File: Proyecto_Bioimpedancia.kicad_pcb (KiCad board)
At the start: 2 copper layers, 100 x 100 mm, 76 parts, among them J1 Jumper, J2 Jumper, J3 Jumper_Calibration, J4 Jumper, J5 Jumper, J6 Jumper, P1 SD_LAPIZ, P10 UNIVERSAL_PINS, P11 SOURCE_2, P12 RESET, P13 POWER, P14 BIO_OUT1, P15 GND_REGULATOR, P16 BIO_OUT2, P17 TOR_1, P18 TOR_2, P19 TOR_3, P2 GPIO, P20 TOR_4, P3 SOURCE_3, P4 SERIAL_VIRTUAL, P5 ENCODER, P6 I2C, P7 CONN_01X04, P8 SOURCE_1, P9 SPI, SW1 SW_PUSH, U1 AD8606, U2 ADG819, U3 Atmega328PA, U4 LD1117S50TR, Y1 XRCHA_16M

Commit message: Logos y Nombre de la Placa
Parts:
- added G***: LOGO, Logos_Fuentes:UIS, F.Cu at (92.7, 121.3)
- added G***: LOGO, Logos_Fuentes:CMOS, F.Cu at (92.9, 111.8)
- added G***: LOGO, Logos_Fuentes:Colombia, F.Cu at (93.0, 131.1)
- added G***: LOGO, Logos_Fuentes:SBS, F.Cu at (152.6, 108.0)
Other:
- board text added: "1 BIOIMPEDANCEMETER"

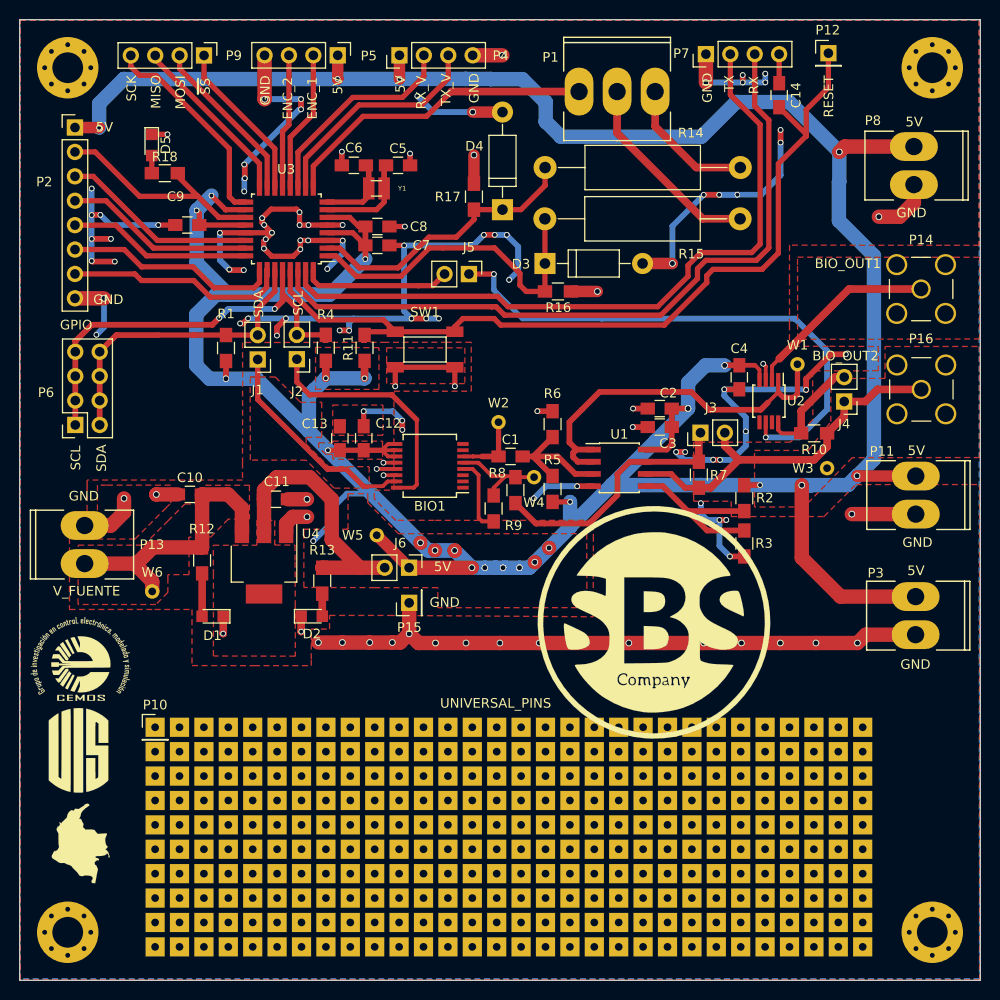
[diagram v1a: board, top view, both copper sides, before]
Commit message: Vias de PCB
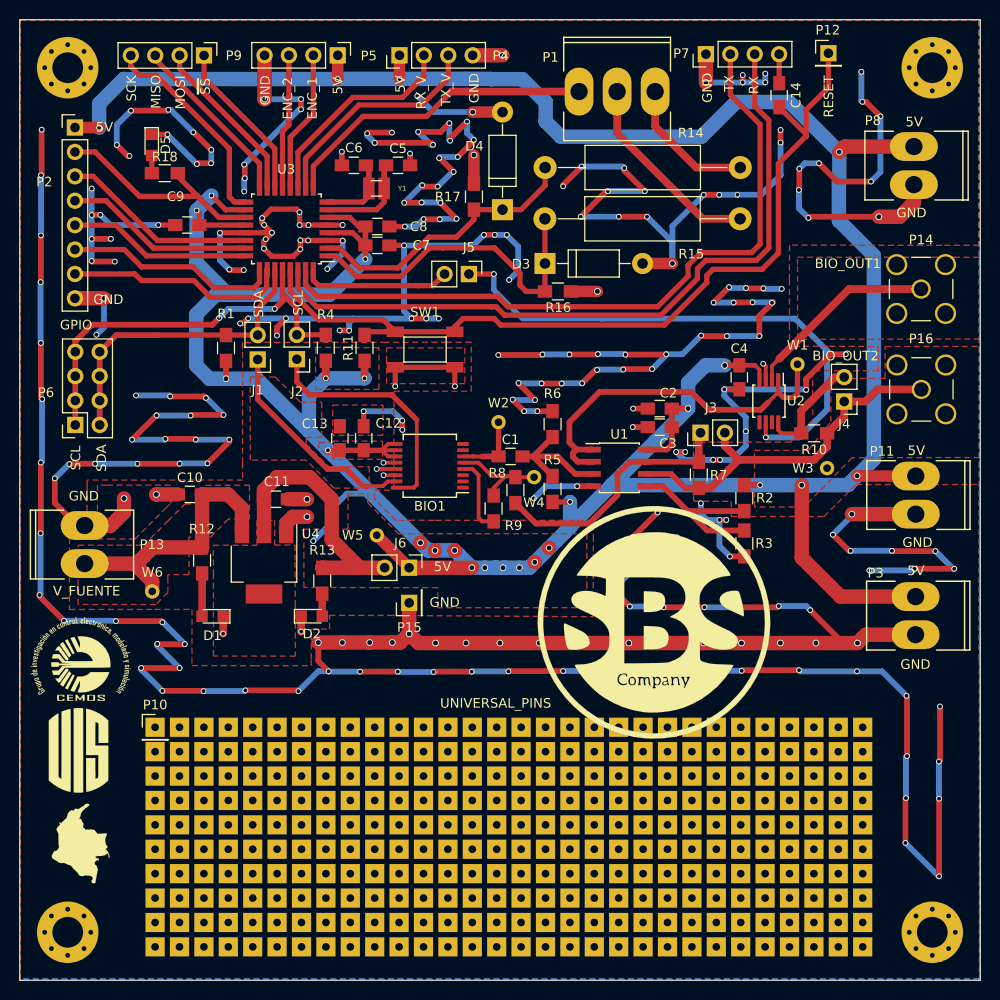
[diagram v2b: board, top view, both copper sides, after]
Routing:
- net /AGND: track 374.4 -> 917.6 mm, vias 118 -> 265
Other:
- board text added: "001 BIOIMPEDANCEMETER"
- board text removed: "1 BIOIMPEDANCEMETER"

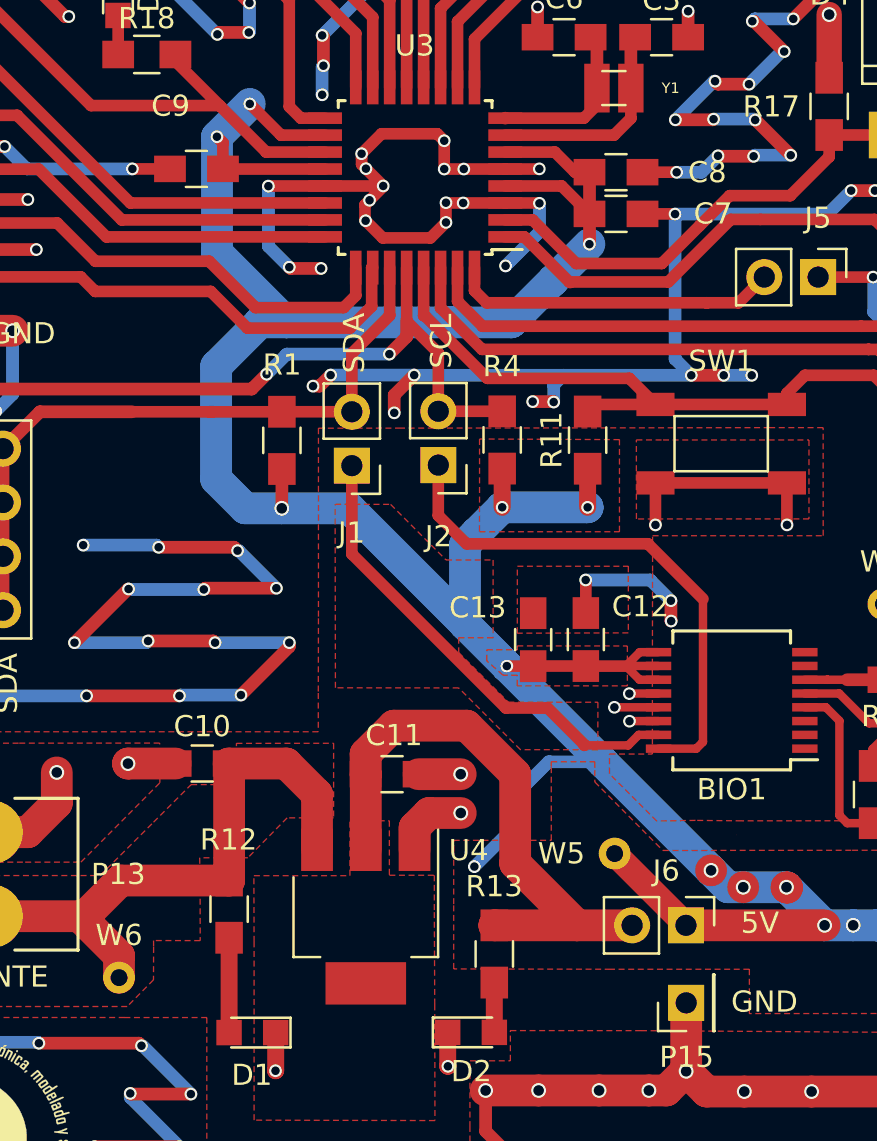
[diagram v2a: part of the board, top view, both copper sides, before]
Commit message: Planos de placa mejorados
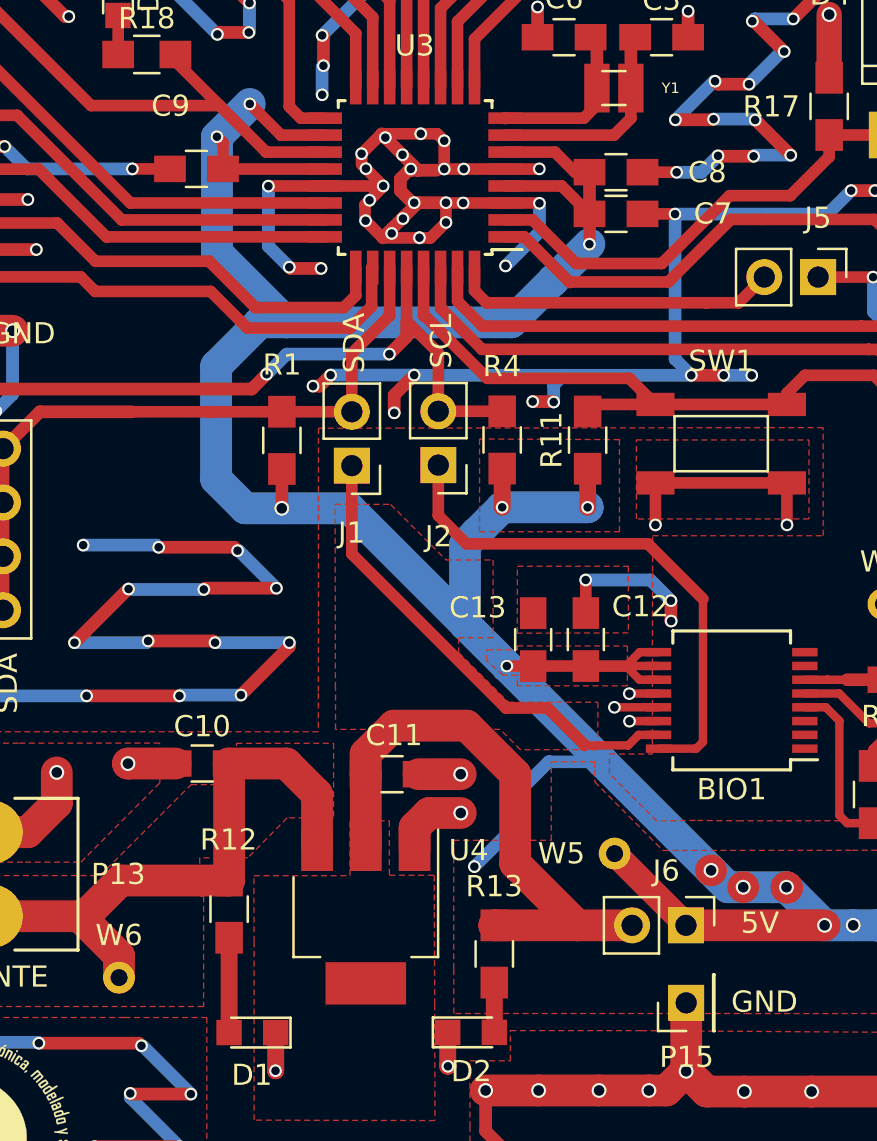
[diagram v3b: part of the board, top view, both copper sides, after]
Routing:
- net /AGND: track 917.6 -> 928.1 mm, vias 265 -> 273
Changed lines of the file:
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@@
     (thickness 1.6)
     (drawings 43)
-    (tracks 1368)
+    (tracks 1406)
     (zones 0)
     (modules 80)
@@
   (segment (start 132.70552 90.67836) (end 133.76438 90.67836) (width 0.4) (layer F.Cu) (net 3))
   (segment (start 133.76438 90.67836) (end 133.7691 90.68308) (width 0.4) (layer F.Cu) (net 3))
+  (via (at 114.53 69.83) (size 0.6) (drill 0.4) (layers F.Cu B.Cu) (net 5))
+  (segment (start 114.53 69.83) (end 114.53 69.85) (width 0.6) (layer B.Cu) (net 5))
+  (segment (start 114.53 69.83) (end 114.53 69.84) (width 0.6) (layer F.Cu) (net 5))
+  (segment (start 114.53 69.83) (end 114.53 69.84) (width 0.6) (layer F.Cu) (net 5))
+  (via (at 114.59 64.93) (size 0.6) (drill 0.4) (layers F.Cu B.Cu) (net 5))
+  (segment (start 114.59 64.93) (end 114.59 64.92) (width 0.6) (layer B.Cu) (net 5))
+  (segment (start 113.22 69.62) (end 113.22 69.63) (width 0.6) (layer B.Cu) (net 5))
+  (via (at 113.22 69.63) (size 0.6) (drill 0.4) (layers F.Cu B.Cu) (net 5))
+  (segment (start 113.22 69.63) (end 113.115 69.525) (width 0.6) (layer F.Cu) (net 5))
+  (segment (start 113.115 69.525) (end 113.22 69.63) (width 0.6) (layer F.Cu) (net 5))
+  (segment (start 113.22 69.63) (end 113.22 69.42) (width 0.6) (layer F.Cu) (net 5))
+  (via (at 112.92 65.11) (size 0.6) (drill 0.4) (layers F.Cu B.Cu) (net 5))
+  (via (at 113.75 68.93) (size 0.6) (drill 0.4) (layers F.Cu B.Cu) (net 5))
+  (segment (start 113.75 68.89) (end 113.75 68.93) (width 0.6) (layer F.Cu) (net 5))
+  (segment (start 113.73 68.91) (end 113.75 68.93) (width 0.6) (layer F.Cu) (net 5))
+  (segment (start 113.75 68.93) (end 113.73 68.91) (width 0.6) (layer F.Cu) (net 5))
+  (via (at 113.73 65.92) (size 0.6) (drill 0.4) (layers F.Cu B.Cu) (net 5))
+  (via (at 114.12 66.59) (size 0.6) (drill 0.4) (layers F.Cu B.Cu) (net 5))
+  (segment (start 114.03 66.65) (end 114.12 66.65) (width 0.6) (layer F.Cu) (net 5))
+  (segment (start 114.12 66.65) (end 114.12 66.59) (width 0.6) (layer F.Cu) (net 5))
+  (via (at 114.28 68.18) (size 0.6) (drill 0.4) (layers F.Cu B.Cu) (net 5))
+  (segment (start 114.28 68.18) (end 114.28 68.17) (width 0.6) (layer B.Cu) (net 5))
+  (segment (start 114.46 68.18) (end 114.28 68.18) (width 0.6) (layer F.Cu) (net 5))
+  (segment (start 114.28 68.18) (end 114.19 68.18) (width 0.6) (layer F.Cu) (net 5))
+  (segment (start 114.03 66.65) (end 114.46 66.65) (width 0.6) (layer F.Cu) (net 5))
+  (segment (start 113.63 67.05) (end 114.03 66.65) (width 0.6) (layer F.Cu) (net 5))
+  (segment (start 113.63 67.62) (end 113.63 67.05) (width 0.6) (layer F.Cu) (net 5))
+  (segment (start 114.19 68.18) (end 113.63 67.62) (width 0.6) (layer F.Cu) (net 5))
+  (segment (start 115.78 68.18) (end 114.46 68.18) (width 0.6) (layer F.Cu) (net 5))
+  (segment (start 114.46 68.18) (end 113.75 68.89) (width 0.6) (layer F.Cu) (net 5))
+  (segment (start 113.75 68.89) (end 113.22 69.42) (width 0.6) (layer F.Cu) (net 5))
+  (segment (start 113.22 69.42) (end 112.8 69.84) (width 0.6) (layer F.Cu) (net 5))
+  (segment (start 115.34 66.65) (end 114.46 66.65) (width 0.6) (layer F.Cu) (net 5))
+  (segment (start 114.46 66.65) (end 113.73 65.92) (width 0.6) (layer F.Cu) (net 5))
+  (segment (start 113.73 65.92) (end 112.92 65.11) (width 0.6) (layer F.Cu) (net 5))
+  (segment (start 112.92 65.11) (end 112.74 64.93) (width 0.6) (layer F.Cu) (net 5))
   (segment (start 173.18736 96.68256) (end 173.18736 96.85264) (width 0.6) (layer B.Cu) (net 5))
   (via (at 173.18736 96.68256) (size 0.7) (drill 0.5) (layers F.Cu B.Cu) (net 5))
@@
   (via (at 139.08 85.97) (size 0.6) (drill 0.4) (layers F.Cu B.Cu) (net 5))
   (segment (start 139.08624 85.96376) (end 139.08 85.97) (width 0.6) (layer B.Cu) (net 5))
-  (segment (start 93.325 97.8688) (end 92.5688 97.8688) (width 0.6) (layer F.Cu) (net 5) (status C00000))
-  (segment (start 92.5688 97.8688) (end 90.22 95.52) (width 0.6) (layer F.Cu) (net 5) (status 400000))
+  (segment (start 93.325 97.8688) (end 92.5688 97.8688) (width 0.6) (layer F.Cu) (net 5))
+  (segment (start 92.5688 97.8688) (end 90.22 95.52) (width 0.6) (layer F.Cu) (net 5))
   (via (at 98.67 84.33) (size 0.6) (drill 0.4) (layers F.Cu B.Cu) (net 5))
   (segment (start 102.13 84.33) (end 98.67 84.33) (width 0.6) (layer B.Cu) (net 5))
@@
   (via (at 111.8 65.87) (size 0.6) (drill 0.4) (layers F.Cu B.Cu) (net 5))
   (via (at 111.99 69.03) (size 0.6) (drill 0.4) (layers F.Cu B.Cu) (net 5))
+  (segment (start 112.175 68.065) (end 111.96 68.28) (width 0.55) (layer F.Cu) (net 5))
+  (segment (start 111.96 68.28) (end 111.96 69) (width 0.55) (layer F.Cu) (net 5))
+  (segment (start 111.99 69.03) (end 112.8 69.84) (width 0.55) (layer F.Cu) (net 5))
+  (segment (start 111.99 69.03) (end 111.96 69) (width 0.55) (layer F.Cu) (net 5))
   (via (at 112.005 66.575) (size 0.6) (drill 0.4) (layers F.Cu B.Cu) (net 5))
   (segment (start 112.005 66.575) (end 112 66.58) (width 0.55) (layer B.Cu) (net 5))
   (via (at 112.175 68.065) (size 0.6) (drill 0.4) (layers F.Cu B.Cu) (net 5))
   (segment (start 112.175 68.065) (end 112.17 68.06) (width 0.55) (layer B.Cu) (net 5))
-  (segment (start 111.99 69.03) (end 111.96 69) (width 0.55) (layer F.Cu) (net 5))
   (segment (start 111.8 66.08) (end 111.8 65.87) (width 0.55) (layer F.Cu) (net 5))
   (via (at 115.6975 65.2575) (size 0.6) (drill 0.4) (layers F.Cu B.Cu) (net 5))
@@
   (segment (start 115.78 69.11) (end 115.78 68.18) (width 0.55) (layer F.Cu) (net 5))
   (segment (start 115.05 69.84) (end 115.78 69.11) (width 0.55) (layer F.Cu) (net 5))
-  (segment (start 112.8 69.84) (end 115.05 69.84) (width 0.55) (layer F.Cu) (net 5))
-  (segment (start 111.99 69.03) (end 112.8 69.84) (width 0.55) (layer F.Cu) (net 5))
-  (segment (start 111.96 68.28) (end 111.96 69) (width 0.55) (layer F.Cu) (net 5))
+  (segment (start 112.8 69.84) (end 114.53 69.84) (width 0.55) (layer F.Cu) (net 5))
+  (segment (start 114.53 69.84) (end 115.05 69.84) (width 0.55) (layer F.Cu) (net 5))
   (segment (start 112.82 67.42) (end 112.175 68.065) (width 0.55) (layer F.Cu) (net 5))
-  (segment (start 112.175 68.065) (end 111.96 68.28) (width 0.55) (layer F.Cu) (net 5))
   (segment (start 115.6975 66.5925) (end 115.6975 65.2575) (width 0.55) (layer F.Cu) (net 5))
   (segment (start 111.8 66.37) (end 112.005 66.575) (width 0.55) (layer F.Cu) (net 5))
@@
   (segment (start 111.8 66.08) (end 111.8 66.37) (width 0.55) (layer F.Cu) (net 5))
   (segment (start 112.74 64.93) (end 111.8 65.87) (width 0.55) (layer F.Cu) (net 5))
-  (segment (start 115.37 64.93) (end 112.74 64.93) (width 0.55) (layer F.Cu) (net 5))
+  (segment (start 115.37 64.93) (end 114.59 64.93) (width 0.55) (layer F.Cu) (net 5))
+  (segment (start 114.59 64.93) (end 112.74 64.93) (width 0.55) (layer F.Cu) (net 5))
   (segment (start 115.6975 65.2575) (end 115.37 64.93) (width 0.55) (layer F.Cu) (net 5))
   (segment (start 115.7925 68.1925) (end 115.78 68.18) (width 0.55) (layer F.Cu) (net 5))
@@
         (xy 115.72494 84.97062) (xy 115.78336 85.02904) (xy 115.783339 85.030205) (xy 118.00332 85.02904) (xy 118.00332 88.6968)
         (xy 116.38026 88.6968) (xy 116.38026 89.39784) (xy 118.7196 91.73718) (xy 122.94616 91.73972) (xy 122.94108 93.97746)
-        (xy 119.29364 93.97746) (xy 116.38026 91.06408) (xy 110.5662 91.059) (xy 110.55096 82.40776) (xy 113.16716 82.40776)
-        (xy 115.72494 84.97062)
+        (xy 119.29364 93.97746) (xy 118.33618 93.02) (xy 110.57 93.02) (xy 110.57 91.059003) (xy 110.5662 91.059)
+        (xy 110.55096 82.40776) (xy 113.16716 82.40776) (xy 115.72494 84.97062)
       )
     )
@@
       (pts
         (xy 110.47984 97.19056) (xy 108.28782 97.1931) (xy 106.43616 99.07524) (xy 104.1654 99.07524) (xy 104.18122 100.495109)
-        (xy 104.18572 100.4951) (xy 104.18572 100.55352) (xy 104.18826 102.98176) (xy 101.98862 102.97922) (xy 101.99116 103.28148)
-        (xy 101.98608 104.83088) (xy 100.74656 106.09072) (xy 92.63888 106.09072) (xy 92.6592 99.91344) (xy 99.46894 99.91344)
+        (xy 104.18572 100.4951) (xy 104.18572 100.55352) (xy 104.186072 100.89) (xy 104.35 100.89) (xy 104.35 106.09)
+        (xy 100.747268 106.09) (xy 100.74656 106.09072) (xy 92.63888 106.09072) (xy 92.6592 99.91344) (xy 99.46894 99.91344)
         (xy 101.98608 97.39884) (xy 103.76154 95.62338) (xy 105.90022 95.62338) (xy 105.89768 93.68028) (xy 110.47984 93.6752)
         (xy 110.47984 97.19056)
@@
     (polygon
       (pts
-        (xy 116.14404 101.26218) (xy 116.14404 98.78568) (xy 116.14404 98.25228) (xy 120.74652 98.25228) (xy 120.74652 94.77756)
-        (xy 120.74652 94.54642) (xy 122.7963 94.54642) (xy 122.79884 94.94012) (xy 122.79884 95.49892) (xy 125.67666 98.39706)
-        (xy 126.0094 98.7298) (xy 134.93242 98.72218) (xy 145.59534 98.71202) (xy 145.60296 103.84536) (xy 145.5928 106.41584)
-        (xy 130.08864 106.42346) (xy 130.08864 104.33304) (xy 123.55068 104.33304) (xy 116.14404 104.3178) (xy 116.14404 101.26218)
+        (xy 122.79884 94.94012) (xy 122.79884 95.49892) (xy 125.67666 98.39706) (xy 126.0094 98.7298) (xy 134.93242 98.72218)
+        (xy 145.59534 98.71202) (xy 145.60296 103.84536) (xy 145.5928 106.41584) (xy 130.08864 106.42346) (xy 130.08864 106.42)
+        (xy 116.15 106.42) (xy 116.15 104.317812) (xy 116.14404 104.3178) (xy 116.14404 98.25228) (xy 120.74652 98.25228)
+        (xy 120.74652 94.54642) (xy 122.7963 94.54642) (xy 122.79884 94.94012)
       )
     )

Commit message: Capacitores de Cristal 0402 cambiados
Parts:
- removed G***: LOGO, Logos_Fuentes:UIS
- removed G***: LOGO, Logos_Fuentes:CMOS
- removed G***: LOGO, Logos_Fuentes:Colombia
- removed G***: LOGO, Logos_Fuentes:SBS
- C5, C6: footprint Capacitors_SMD:C_0805_HandSoldering -> Capacitors_SMD:C_0402
- moved C6 1.00 mm to (122.3, 60.4)
- moved C5 0.90 mm to (125.0, 60.4)
